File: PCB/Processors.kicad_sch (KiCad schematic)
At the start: 0 parts

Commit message: new file:   Datasheet/HMC849A_RF_Switch_SPDT.pdf 	new file:   Datasheet/TG2016SMN_26MHz_MCGNNM_Oscillator.pdf 	modified:   PCB/DroidRadio.kicad_pro 	modified:   PCB/DroidRadio.kicad_sch 	modified:   PCB/Processors.kicad_sch 	modified:   PCB/Simulation/Transmitter_Side.pll 	modified:   PCB/Transmitter.kicad_sch 	deleted:    PCB/~DroidRadio.kicad_pro.lck
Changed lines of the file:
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@@
 	(generator_version "10.0")
 	(paper "A4")
+	(global_label "SYN_LD"
+		(shape input)
+		(at 66.04 67.31 180)
+		(fields_autoplaced yes)
+		(effects
+			(font
+				(size 1.27 1.27)
+			)
+			(justify right)
+		)
+		(property "Intersheetrefs" "${INTERSHEET_REFS}"
+			(at 56.1605 67.31 0)
+			(hide yes)
+			(show_name no)
+			(do_not_autoplace no)
+			(effects
+				(font
+					(size 1.27 1.27)
+				)
+				(justify right)
+			)
+		)
+	)
 	(global_label "SYN_CE"
 		(shape input)
@@
 			(hide yes)
 			(show_name no)
+			(do_not_autoplace no)
+			(effects
+				(font
+					(size 1.27 1.27)
+				)
+				(justify right)
+			)
+		)
+	)
+	(global_label "SYN_MUXOUT"
+		(shape input)
+		(at 66.04 69.85 180)
+		(fields_autoplaced yes)
+		(effects
+			(font
+				(size 1.27 1.27)
+			)
+			(justify right)
+		)
+		(property "Intersheetrefs" "${INTERSHEET_REFS}"
+			(at 50.8386 69.85 0)
+			(hide yes)
+			(show_name no)

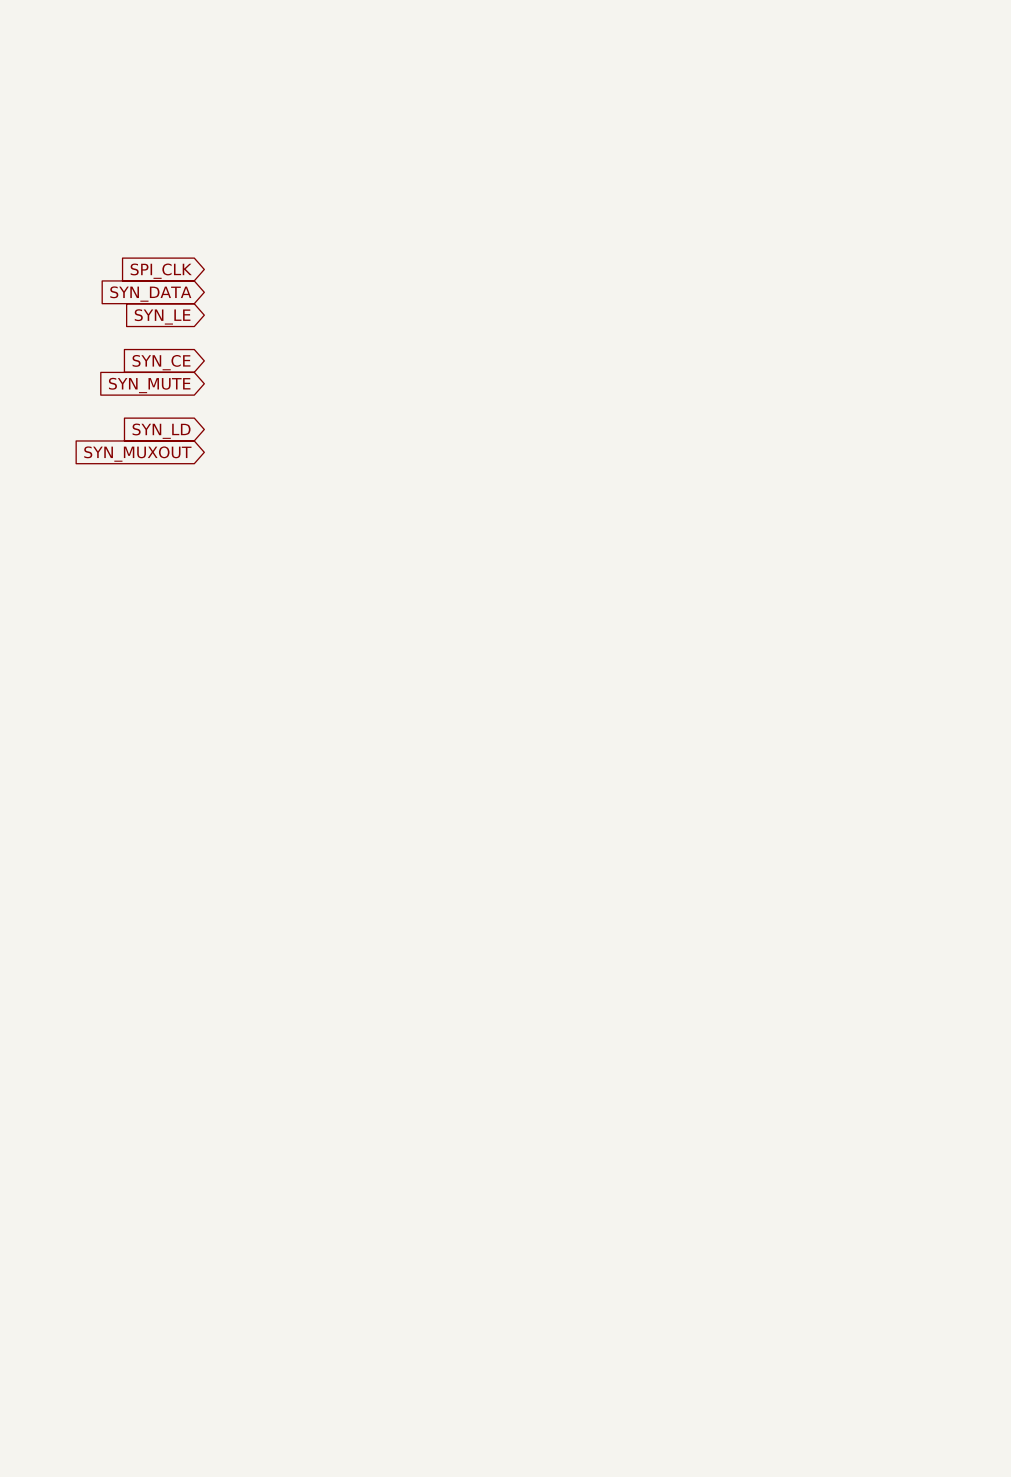
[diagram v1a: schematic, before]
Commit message: Add datasheets and update PCB schematics
Add LFCN-1400+ and LFCN-2000+ low-pass filter datasheets, plus STM32H43VI MCU and TMP411 temperature sensor datasheets. Update DroidRadio.kicad_pro, Processors.kicad_sch and Transmitter.kicad_sch.
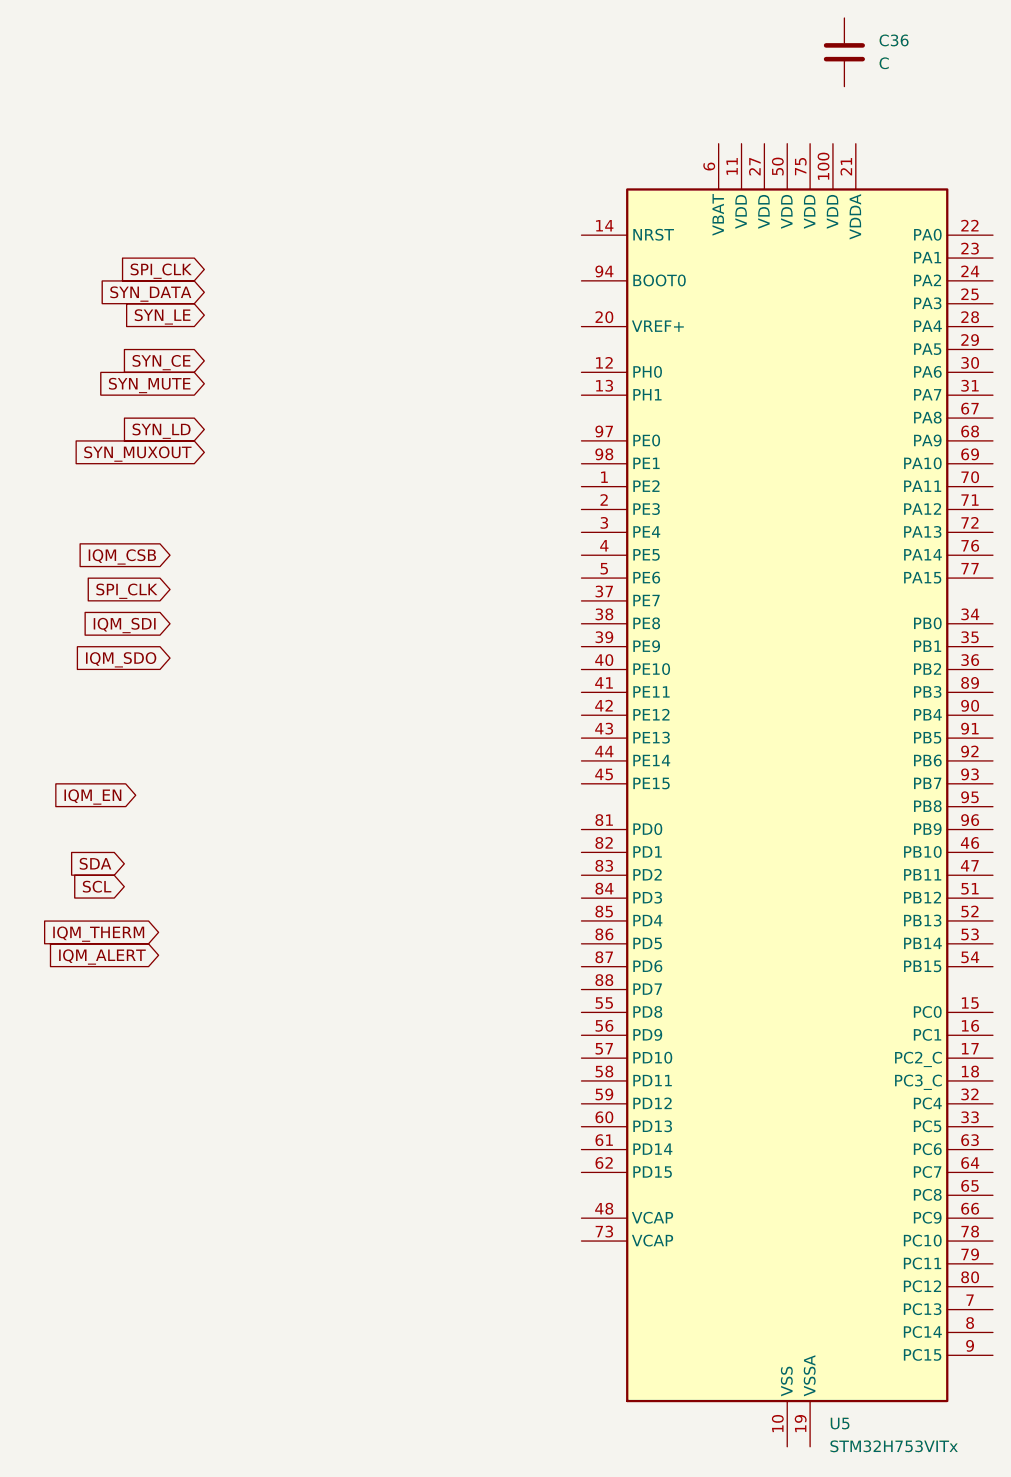
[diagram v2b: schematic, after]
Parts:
- added C36: C, Package_QFP:LQFP-100_14x14mm_P0.5mm, symbol Device:C
- added U5: STM32H753VITx, Package_QFP:LQFP-100_14x14mm_P0.5mm, symbol MCU_ST_STM32H7:STM32H753VITx
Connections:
- new net: U5.10 (VSS), U5.26 (VSS), U5.49 (VSS), U5.74 (VSS), U5.99 (VSS)

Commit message: Updated PCB schematics, added new datasheet and components library
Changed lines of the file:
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@@
 	(global_label "SYN_LD"
 		(shape input)
-		(at 66.04 67.31 180)
-		(fields_autoplaced yes)
-		(effects
-			(font
-				(size 1.27 1.27)
-			)
-			(justify right)
-		)
-		(property "Intersheetrefs" "${INTERSHEET_REFS}"
-			(at 56.1605 67.31 0)
+		(at 91.44 86.36 180)
+		(fields_autoplaced yes)
+		(effects
+			(font
+				(size 1.27 1.27)
+			)
+			(justify right)
+		)
+		(property "Intersheetrefs" "${INTERSHEET_REFS}"
+			(at 81.5605 86.36 0)
 			(hide yes)
 			(show_name no)
@@
 	(global_label "SYN_CE"
 		(shape input)
-		(at 66.04 59.69 180)
-		(fields_autoplaced yes)
-		(effects
-			(font
-				(size 1.27 1.27)
-			)
-			(justify right)
-		)
-		(property "Intersheetrefs" "${INTERSHEET_REFS}"
-			(at 56.0396 59.69 0)
+		(at 91.44 78.74 180)
+		(fields_autoplaced yes)
+		(effects
+			(font
+				(size 1.27 1.27)
+			)
+			(justify right)
+		)
+		(property "Intersheetrefs" "${INTERSHEET_REFS}"
+			(at 81.4396 78.74 0)
 			(hide yes)
 			(show_name no)
@@
 	(global_label "SDA"
 		(shape input)
-		(at 57.15 115.57 180)
-		(fields_autoplaced yes)
-		(effects
-			(font
-				(size 1.27 1.27)
-			)
-			(justify right)
-		)
-		(property "Intersheetrefs" "${INTERSHEET_REFS}"
-			(at 50.5967 115.57 0)
+		(at 90.17 115.57 180)
+		(fields_autoplaced yes)
+		(effects
+			(font
+				(size 1.27 1.27)
+			)
+			(justify right)
+		)
+		(property "Intersheetrefs" "${INTERSHEET_REFS}"
+			(at 83.6167 115.57 0)
 			(hide yes)
 			(show_name no)
@@
 	(global_label "IQM_THERM"
 		(shape input)
-		(at 60.96 123.19 180)
-		(fields_autoplaced yes)
-		(effects
-			(font
-				(size 1.27 1.27)
-			)
-			(justify right)
-		)
-		(property "Intersheetrefs" "${INTERSHEET_REFS}"
-			(at 47.452 123.19 0)
+		(at 90.17 123.19 180)
+		(fields_autoplaced yes)
+		(effects
+			(font
+				(size 1.27 1.27)
+			)
+			(justify right)
+		)
+		(property "Intersheetrefs" "${INTERSHEET_REFS}"
+			(at 76.662 123.19 0)
 			(hide yes)
 			(show_name no)
@@
 	(global_label "SYN_LE"
 		(shape input)
-		(at 66.04 54.61 180)
-		(fields_autoplaced yes)
-		(effects
-			(font
-				(size 1.27 1.27)
-			)
-			(justify right)
-		)
-		(property "Intersheetrefs" "${INTERSHEET_REFS}"
-			(at 56.2815 54.61 0)
+		(at 91.44 73.66 180)
+		(fields_autoplaced yes)
+		(effects
+			(font
+				(size 1.27 1.27)
+			)
+			(justify right)
+		)
+		(property "Intersheetrefs" "${INTERSHEET_REFS}"
+			(at 81.6815 73.66 0)
 			(hide yes)
 			(show_name no)
@@
 	(global_label "SYN_DATA"
 		(shape input)
-		(at 66.04 52.07 180)
-		(fields_autoplaced yes)
-		(effects
-			(font
-				(size 1.27 1.27)
-			)
-			(justify right)
-		)
-		(property "Intersheetrefs" "${INTERSHEET_REFS}"
-			(at 54.0438 52.07 0)
+		(at 91.44 71.12 180)
+		(fields_autoplaced yes)
+		(effects
+			(font
+				(size 1.27 1.27)
+			)
+			(justify right)
+		)
+		(property "Intersheetrefs" "${INTERSHEET_REFS}"
+			(at 79.4438 71.12 0)
 			(hide yes)
 			(show_name no)
@@
 	(global_label "SPI_CLK"
 		(shape input)
-		(at 62.23 85.09 180)
-		(fields_autoplaced yes)
-		(effects
-			(font
-				(size 1.27 1.27)
-			)
-			(justify right)
-		)
-		(property "Intersheetrefs" "${INTERSHEET_REFS}"
-			(at 51.6248 85.09 0)
+		(at 91.44 97.79 180)
+		(fields_autoplaced yes)
+		(effects
+			(font
+				(size 1.27 1.27)
+			)
+			(justify right)
+		)
+		(property "Intersheetrefs" "${INTERSHEET_REFS}"
+			(at 80.8348 97.79 0)
 			(hide yes)
 			(show_name no)
@@
 	(global_label "SYN_MUTE"
 		(shape input)
-		(at 66.04 62.23 180)
-		(fields_autoplaced yes)
-		(effects
-			(font
-				(size 1.27 1.27)
-			)
-			(justify right)
-		)
-		(property "Intersheetrefs" "${INTERSHEET_REFS}"
-			(at 53.5601 62.23 0)
+		(at 91.44 81.28 180)
+		(fields_autoplaced yes)
+		(effects
+			(font
+				(size 1.27 1.27)
+			)
+			(justify right)
+		)
+		(property "Intersheetrefs" "${INTERSHEET_REFS}"
+			(at 78.9601 81.28 0)
 			(hide yes)
 			(show_name no)
@@
 	(global_label "IQM_SDI"
 		(shape input)
-		(at 62.23 88.9 180)
-		(fields_autoplaced yes)
-		(effects
-			(font
-				(size 1.27 1.27)
-			)
-			(justify right)
-		)
-		(property "Intersheetrefs" "${INTERSHEET_REFS}"
-			(at 51.8062 88.9 0)
+		(at 91.44 101.6 180)
+		(fields_autoplaced yes)
+		(effects
+			(font
+				(size 1.27 1.27)
+			)
+			(justify right)
+		)
+		(property "Intersheetrefs" "${INTERSHEET_REFS}"
+			(at 81.0162 101.6 0)
 			(hide yes)
 			(show_name no)
@@
 	(global_label "IQM_EN"
 		(shape input)
-		(at 58.42 107.95 180)
-		(fields_autoplaced yes)
-		(effects
-			(font
-				(size 1.27 1.27)
-			)
-			(justify right)
-		)
-		(property "Intersheetrefs" "${INTERSHEET_REFS}"
-			(at 48.601 107.95 0)
+		(at 91.44 110.49 180)
+		(fields_autoplaced yes)
+		(effects
+			(font
+				(size 1.27 1.27)
+			)
+			(justify right)
+		)
+		(property "Intersheetrefs" "${INTERSHEET_REFS}"
+			(at 81.621 110.49 0)
 			(hide yes)
 			(show_name no)
@@
 	(global_label "IQM_ALERT"
 		(shape input)
-		(at 60.96 125.73 180)
-		(fields_autoplaced yes)
-		(effects
-			(font
-				(size 1.27 1.27)
-			)
-			(justify right)
-		)
-		(property "Intersheetrefs" "${INTERSHEET_REFS}"
-			(at 48.1172 125.73 0)
+		(at 90.17 125.73 180)
+		(fields_autoplaced yes)
+		(effects
+			(font
+				(size 1.27 1.27)
+			)
+			(justify right)
+		)
+		(property "Intersheetrefs" "${INTERSHEET_REFS}"
+			(at 77.3272 125.73 0)
 			(hide yes)
 			(show_name no)
@@
 	(global_label "SCL"
 		(shape input)
-		(at 57.15 118.11 180)
-		(fields_autoplaced yes)
-		(effects
-			(font
-				(size 1.27 1.27)
-			)
-			(justify right)
-		)
-		(property "Intersheetrefs" "${INTERSHEET_REFS}"
-			(at 50.6572 118.11 0)
+		(at 90.17 118.11 180)
+		(fields_autoplaced yes)
+		(effects
+			(font
+				(size 1.27 1.27)
+			)
+			(justify right)
+		)
+		(property "Intersheetrefs" "${INTERSHEET_REFS}"
+			(at 83.6772 118.11 0)
 			(hide yes)
 			(show_name no)
@@
 	(global_label "SYN_MUXOUT"
 		(shape input)
-		(at 66.04 69.85 180)
-		(fields_autoplaced yes)
-		(effects
-			(font
-				(size 1.27 1.27)
-			)
-			(justify right)
-		)
-		(property "Intersheetrefs" "${INTERSHEET_REFS}"
-			(at 50.8386 69.85 0)
+		(at 91.44 88.9 180)
+		(fields_autoplaced yes)
+		(effects
+			(font
+				(size 1.27 1.27)
+			)
+			(justify right)
+		)
+		(property "Intersheetrefs" "${INTERSHEET_REFS}"
+			(at 76.2386 88.9 0)
 			(hide yes)
 			(show_name no)
@@
 	(global_label "IQM_CSB"
 		(shape input)
-		(at 62.23 81.28 180)
-		(fields_autoplaced yes)
-		(effects
-			(font
-				(size 1.27 1.27)
-			)
-			(justify right)
-		)
-		(property "Intersheetrefs" "${INTERSHEET_REFS}"
-			(at 51.141 81.28 0)
+		(at 91.44 93.98 180)
+		(fields_autoplaced yes)
+		(effects
+			(font
+				(size 1.27 1.27)
+			)
+			(justify right)
+		)
+		(property "Intersheetrefs" "${INTERSHEET_REFS}"
+			(at 80.351 93.98 0)
 			(hide yes)
 			(show_name no)
@@
 	(global_label "IQM_SDO"
 		(shape input)
-		(at 62.23 92.71 180)
-		(fields_autoplaced yes)
-		(effects
-			(font
-				(size 1.27 1.27)
-			)
-			(justify right)
-		)
-		(property "Intersheetrefs" "${INTERSHEET_REFS}"
-			(at 51.0805 92.71 0)
+		(at 91.44 105.41 180)
+		(fields_autoplaced yes)
+		(effects
+			(font
+				(size 1.27 1.27)
+			)
+			(justify right)
+		)
+		(property "Intersheetrefs" "${INTERSHEET_REFS}"
+			(at 80.2905 105.41 0)
 			(hide yes)
 			(show_name no)
@@
 	(global_label "SPI_CLK"
 		(shape input)
-		(at 66.04 49.53 180)
-		(fields_autoplaced yes)
-		(effects
-			(font
-				(size 1.27 1.27)
-			)
-			(justify right)
-		)
-		(property "Intersheetrefs" "${INTERSHEET_REFS}"
-			(at 55.4348 49.53 0)
-			(hide yes)
-			(show_name no)
+		(at 91.44 68.58 180)
+		(fields_autoplaced yes)
+		(effects
+			(font
+				(size 1.27 1.27)
+			)
+			(justify right)
+		)
+		(property "Intersheetrefs" "${INTERSHEET_REFS}"
+			(at 80.8348 68.58 0)
+			(hide yes)
+			(show_name no)
